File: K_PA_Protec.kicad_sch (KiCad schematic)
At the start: 89 parts, among them IC1 MCP23017_SO, J1 IDC 10 Straight, J10 MH2, J11 MH3, J12 MH4, J13 MH5, J14 MH6, J2 Molex KK 4, J3 IDC 10 Straight, J4 Molex KK 2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

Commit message: routing, first stage
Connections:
- net GND: now also SW1.2C, SW1.S1; no longer SW1.1C, SW1.S2
- net at J2.1 (Pin_1), R23.2: now also SW1.2A; no longer SW1.1A
- net at J2.2 (Pin_2), R5.2: now also SW1.2B; no longer SW1.1B
- net at J2.3 (Pin_3): now also SW1.S2; no longer SW1.S1
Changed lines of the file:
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@@
     (stroke (width 0) (type default) (color 0 0 0 0))
   )
-  (wire (pts (xy 55.245 186.69) (xy 56.515 186.69))
+  (wire (pts (xy 55.245 186.69) (xy 53.34 186.69))
     (stroke (width 0) (type default) (color 0 0 0 0))
   )
@@
     (stroke (width 0) (type default) (color 0 0 0 0))
   )
-  (wire (pts (xy 61.595 188.595) (xy 61.595 186.69))
-    (stroke (width 0) (type default) (color 0 0 0 0))
-  )
   (wire (pts (xy 131.445 17.78) (xy 132.715 17.78))
     (stroke (width 0) (type default) (color 0 0 0 0))
   )
+  (wire (pts (xy 41.91 188.595) (xy 60.325 188.595))
+    (stroke (width 0) (type default) (color 0 0 0 0))
+  )
   (wire (pts (xy 133.35 86.995) (xy 133.35 87.63))
     (stroke (width 0) (type default) (color 0 0 0 0))
@@
     (stroke (width 0) (type default) (color 0 0 0 0))
   )
+  (wire (pts (xy 60.325 186.69) (xy 60.325 188.595))
+    (stroke (width 0) (type default) (color 0 0 0 0))
+  )
   (wire (pts (xy 34.925 33.02) (xy 34.925 34.29))
     (stroke (width 0) (type default) (color 0 0 0 0))
@@
   )
   (wire (pts (xy 165.1 150.495) (xy 170.18 150.495))
-    (stroke (width 0) (type default) (color 0 0 0 0))
-  )
-  (wire (pts (xy 41.91 188.595) (xy 61.595 188.595))
     (stroke (width 0) (type default) (color 0 0 0 0))
   )
@@
     (pin "1")
   )
-  (symbol (lib_id "RotaryEncoder_Dual_Alps_EC11E-Switch_Vertical_H20mm:RotaryEncoder_Dual_Switch") (at 59.055 179.07 0) (unit 1)
-    (in_bom yes) (on_board yes) (fields_autoplaced)
-    (property "Reference" "SW1" (id 0) (at 59.055 170.0235 0))
-    (property "Value" "RotaryEncoder_Dual_Switch" (id 1) (at 59.055 172.7986 0))
-    (property "Footprint" "RotaryEncoder_Dual_Alps_EC11E-Switch_Vertical_H20mm:RotaryEncoder_Dual_Alps_EC11E-Switch_Vertical_H20mm" (id 2) (at 55.245 175.006 0)
-      (effects (font (size 1.27 1.27)) hide)
-    )
-    (property "Datasheet" "~" (id 3) (at 59.055 172.466 0)
+  (symbol (lib_id "RotaryEncoder_Dual_Alps_EC11E-Switch_Vertical_H20mm:RotaryEncoder_Dual_Switch") (at 57.785 179.07 0) (mirror y) (unit 1)
+    (in_bom yes) (on_board yes) (fields_autoplaced)
+    (property "Reference" "SW1" (id 0) (at 57.785 170.0235 0))
+    (property "Value" "RotaryEncoder_Dual_Switch" (id 1) (at 57.785 172.7986 0))
+    (property "Footprint" "RotaryEncoder_Dual_Alps_EC11E-Switch_Vertical_H20mm:RotaryEncoder_Dual_Alps_EC11E-Switch_Vertical_H20mm" (id 2) (at 61.595 175.006 0)
+      (effects (font (size 1.27 1.27)) hide)
+    )
+    (property "Datasheet" "~" (id 3) (at 57.785 172.466 0)
       (effects (font (size 1.27 1.27)) hide)
     )
@@
     (pin "9")
   )
-  (symbol (lib_id "power:GND") (at 55.245 186.69 270) (unit 1)
-    (in_bom yes) (on_board yes) (fields_autoplaced)
-    (property "Reference" "#PWR0173" (id 0) (at 48.895 186.69 0)
-      (effects (font (size 1.27 1.27)) hide)
-    )
-    (property "Value" "GND" (id 1) (at 55.88 187.169 90)
+  (symbol (lib_id "power:GND") (at 53.34 186.69 270) (mirror x) (unit 1)
+    (in_bom yes) (on_board yes) (fields_autoplaced)
+    (property "Reference" "#PWR0173" (id 0) (at 46.99 186.69 0)
+      (effects (font (size 1.27 1.27)) hide)
+    )
+    (property "Value" "GND" (id 1) (at 53.975 186.211 90)
       (effects (font (size 1.27 1.27)) (justify left))
     )
-    (property "Footprint" "" (id 2) (at 55.245 186.69 0)
-      (effects (font (size 1.27 1.27)) hide)
-    )
-    (property "Datasheet" "" (id 3) (at 55.245 186.69 0)
-      (effects (font (size 1.27 1.27)) hide)
-    )
+    (property "Footprint" "" (id 2) (at 53.34 186.69 0)
+      (effects (font (size 1.27 1.27)) hide)
+    )
+    (property "Datasheet" "" (id 3) (at 53.34 186.69 0)
+      (effects (font (size 1.27 1.27)) hide)
+    )

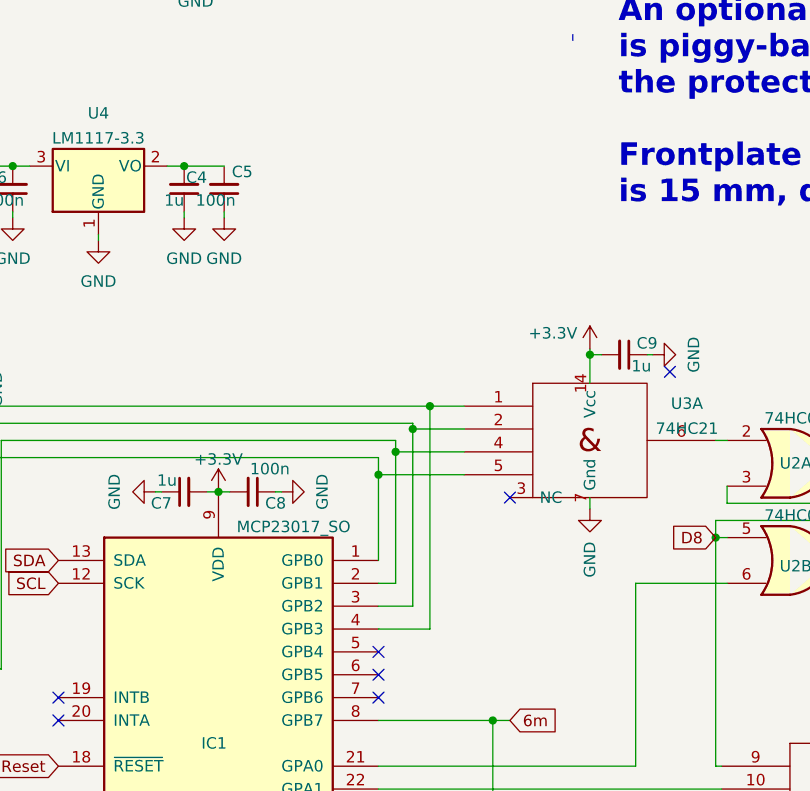
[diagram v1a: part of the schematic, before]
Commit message: routing completed, some minor changes expected
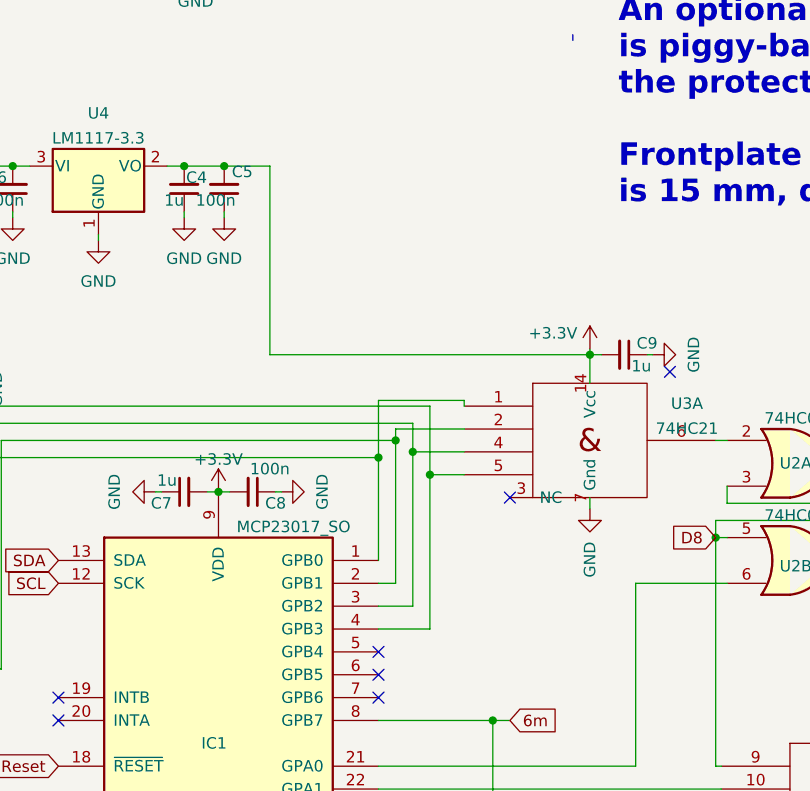
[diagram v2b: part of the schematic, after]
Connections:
- net +3V3: now also C4.2, C5.2, U4.2 (VO)
- net at IC1.3 (GPB2), R3.1, U1.13: now also U3.4; no longer U3.2
- net at IC1.2 (GPB1), R2.1, U1.1: now also U3.2; no longer U3.4
- net at IC1.1 (GPB0), R1.1, U1.2: now also U3.1; no longer U3.5
- net at IC1.4 (GPB3), R4.1, U1.14: now also U3.5; no longer U3.1
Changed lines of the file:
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@@
   (junction (at 41.91 133.985) (diameter 0) (color 0 0 0 0)
   )
-  (junction (at 135.255 85.09) (diameter 0) (color 0 0 0 0)
-  )
   (junction (at 45.72 141.605) (diameter 0) (color 0 0 0 0)
   )
@@
   (junction (at 234.95 27.305) (diameter 0) (color 0 0 0 0)
   )
-  (junction (at 129.54 92.71) (diameter 0) (color 0 0 0 0)
+  (junction (at 112.395 58.42) (diameter 0) (color 0 0 0 0)
+  )
+  (junction (at 133.35 90.17) (diameter 0) (color 0 0 0 0)
   )
   (junction (at 252.095 32.385) (diameter 0) (color 0 0 0 0)
@@
   (junction (at 46.355 119.38) (diameter 0) (color 0 0 0 0)
   )
+  (junction (at 129.54 90.805) (diameter 0) (color 0 0 0 0)
+  )
   (junction (at 142.24 120.015) (diameter 0) (color 0 0 0 0)
   )
@@
   (junction (at 84.455 58.42) (diameter 0) (color 0 0 0 0)
   )
+  (junction (at 135.255 92.71) (diameter 0) (color 0 0 0 0)
+  )
   (junction (at 243.205 32.385) (diameter 0) (color 0 0 0 0)
   )
@@
   (junction (at 49.53 103.505) (diameter 0) (color 0 0 0 0)
   )
-  (junction (at 133.35 87.63) (diameter 0) (color 0 0 0 0)
-  )
   (junction (at 107.95 58.42) (diameter 0) (color 0 0 0 0)
   )
-  (junction (at 131.445 90.17) (diameter 0) (color 0 0 0 0)
-  )
   (junction (at 134.62 149.225) (diameter 0) (color 0 0 0 0)
   )
@@
   )
   (junction (at 43.18 176.53) (diameter 0) (color 0 0 0 0)
+  )
+  (junction (at 131.445 88.9) (diameter 0) (color 0 0 0 0)
   )
   (junction (at 78.74 58.42) (diameter 0) (color 0 0 0 0)
@@
     (stroke (width 0) (type default) (color 0 0 0 0))
   )
-  (wire (pts (xy 133.35 87.63) (xy 139.065 87.63))
-    (stroke (width 0) (type default) (color 0 0 0 0))
-  )
   (wire (pts (xy 267.97 91.44) (xy 276.86 91.44))
     (stroke (width 0) (type default) (color 0 0 0 0))
@@
     (stroke (width 0) (type default) (color 0 0 0 0))
   )
+  (wire (pts (xy 133.35 90.17) (xy 139.065 90.17))
+    (stroke (width 0) (type default) (color 0 0 0 0))
+  )
   (wire (pts (xy 140.335 130.175) (xy 144.145 130.175))
     (stroke (width 0) (type default) (color 0 0 0 0))
@@
     (stroke (width 0) (type default) (color 0 0 0 0))
   )
-  (wire (pts (xy 131.445 90.17) (xy 139.065 90.17))
-    (stroke (width 0) (type default) (color 0 0 0 0))
-  )
   (wire (pts (xy 153.035 79.375) (xy 153.035 78.74))
     (stroke (width 0) (type default) (color 0 0 0 0))
@@
     (stroke (width 0) (type default) (color 0 0 0 0))
   )
-  (wire (pts (xy 135.255 85.09) (xy 139.065 85.09))
-    (stroke (width 0) (type default) (color 0 0 0 0))
-  )
   (wire (pts (xy 129.54 130.175) (xy 140.335 130.175))
     (stroke (width 0) (type default) (color 0 0 0 0))
@@
     (stroke (width 0) (type default) (color 0 0 0 0))
   )
+  (wire (pts (xy 117.475 58.42) (xy 117.475 79.375))
+    (stroke (width 0) (type default) (color 0 0 0 0))
+  )
   (wire (pts (xy 87.63 88.9) (xy 131.445 88.9))
     (stroke (width 0) (type default) (color 0 0 0 0))
   )
+  (wire (pts (xy 129.54 84.455) (xy 129.54 90.805))
+    (stroke (width 0) (type default) (color 0 0 0 0))
+  )
   (wire (pts (xy 130.81 142.875) (xy 144.145 142.875))
     (stroke (width 0) (type default) (color 0 0 0 0))
@@
     (stroke (width 0) (type default) (color 0 0 0 0))
   )
+  (wire (pts (xy 139.065 85.09) (xy 139.065 84.455))
+    (stroke (width 0) (type default) (color 0 0 0 0))
+  )
   (wire (pts (xy 231.775 24.765) (xy 236.855 24.765))
     (stroke (width 0) (type default) (color 0 0 0 0))
@@
     (stroke (width 0) (type default) (color 0 0 0 0))
   )
+  (wire (pts (xy 133.35 90.17) (xy 133.35 107.315))
+    (stroke (width 0) (type default) (color 0 0 0 0))
+  )
   (wire (pts (xy 195.58 120.65) (xy 195.58 128.905))
     (stroke (width 0) (type default) (color 0 0 0 0))
@@
     (stroke (width 0) (type default) (color 0 0 0 0))
   )
-  (wire (pts (xy 133.35 87.63) (xy 133.35 107.315))
+  (wire (pts (xy 133.35 86.995) (xy 133.35 90.17))
     (stroke (width 0) (type default) (color 0 0 0 0))
   )
@@
     (stroke (width 0) (type default) (color 0 0 0 0))
   )
-  (wire (pts (xy 135.255 85.09) (xy 135.255 109.855))
+  (wire (pts (xy 135.255 85.09) (xy 135.255 92.71))
     (stroke (width 0) (type default) (color 0 0 0 0))
   )
@@
     (stroke (width 0) (type default) (color 0 0 0 0))
   )
+  (wire (pts (xy 139.065 87.63) (xy 131.445 87.63))
+    (stroke (width 0) (type default) (color 0 0 0 0))
+  )
   (wire (pts (xy 131.445 36.83) (xy 132.715 36.83))
     (stroke (width 0) (type default) (color 0 0 0 0))
@@
     (stroke (width 0) (type default) (color 0 0 0 0))
   )
-  (wire (pts (xy 129.54 92.71) (xy 139.065 92.71))
-    (stroke (width 0) (type default) (color 0 0 0 0))
-  )
   (wire (pts (xy 83.82 156.845) (xy 83.82 85.09))
     (stroke (width 0) (type default) (color 0 0 0 0))
@@
     (stroke (width 0) (type default) (color 0 0 0 0))
   )
+  (wire (pts (xy 131.445 87.63) (xy 131.445 88.9))
+    (stroke (width 0) (type default) (color 0 0 0 0))
+  )
   (wire (pts (xy 41.91 188.595) (xy 60.325 188.595))
     (stroke (width 0) (type default) (color 0 0 0 0))
   )
-  (wire (pts (xy 133.35 86.995) (xy 133.35 87.63))
-    (stroke (width 0) (type default) (color 0 0 0 0))
-  )
   (wire (pts (xy 93.98 142.875) (xy 93.98 143.51))
     (stroke (width 0) (type default) (color 0 0 0 0))
@@
     (stroke (width 0) (type default) (color 0 0 0 0))
   )
-  (wire (pts (xy 129.54 90.805) (xy 129.54 92.71))
-    (stroke (width 0) (type default) (color 0 0 0 0))
-  )
-  (wire (pts (xy 129.54 92.71) (xy 129.54 102.235))
+  (wire (pts (xy 129.54 90.805) (xy 129.54 102.235))
     (stroke (width 0) (type default) (color 0 0 0 0))
   )
@@
     (stroke (width 0) (type default) (color 0 0 0 0))
   )
+  (wire (pts (xy 135.255 92.71) (xy 139.065 92.71))
+    (stroke (width 0) (type default) (color 0 0 0 0))
+  )
   (wire (pts (xy 37.465 93.345) (xy 37.465 90.805))
     (stroke (width 0) (type default) (color 0 0 0 0))
@@
     (stroke (width 0) (type default) (color 0 0 0 0))
   )
+  (wire (pts (xy 135.255 92.71) (xy 135.255 109.855))
+    (stroke (width 0) (type default) (color 0 0 0 0))
+  )
   (wire (pts (xy 88.9 58.42) (xy 90.805 58.42))
     (stroke (width 0) (type default) (color 0 0 0 0))
@@
     (stroke (width 0) (type default) (color 0 0 0 0))
   )
+  (wire (pts (xy 112.395 58.42) (xy 117.475 58.42))
+    (stroke (width 0) (type default) (color 0 0 0 0))
+  )
   (wire (pts (xy 76.835 106.68) (xy 76.835 128.905))
     (stroke (width 0) (type default) (color 0 0 0 0))
   )
+  (wire (pts (xy 117.475 79.375) (xy 153.035 79.375))
+    (stroke (width 0) (type default) (color 0 0 0 0))
+  )
   (wire (pts (xy 107.95 63.5) (xy 107.95 64.135))
     (stroke (width 0) (type default) (color 0 0 0 0))
@@
     (stroke (width 0) (type default) (color 0 0 0 0))
   )
+  (wire (pts (xy 139.065 84.455) (xy 129.54 84.455))
+    (stroke (width 0) (type default) (color 0 0 0 0))
+  )
   (wire (pts (xy 241.935 40.005) (xy 242.57 40.005))
     (stroke (width 0) (type default) (color 0 0 0 0))
@@
     (stroke (width 0) (type default) (color 0 0 0 0))
   )
-  (wire (pts (xy 131.445 90.17) (xy 131.445 104.775))
+  (wire (pts (xy 131.445 88.9) (xy 131.445 104.775))
     (stroke (width 0) (type default) (color 0 0 0 0))
   )
@@
     (stroke (width 0) (type default) (color 0 0 0 0))
   )
-  (wire (pts (xy 131.445 88.9) (xy 131.445 90.17))
-    (stroke (width 0) (type default) (color 0 0 0 0))
-  )

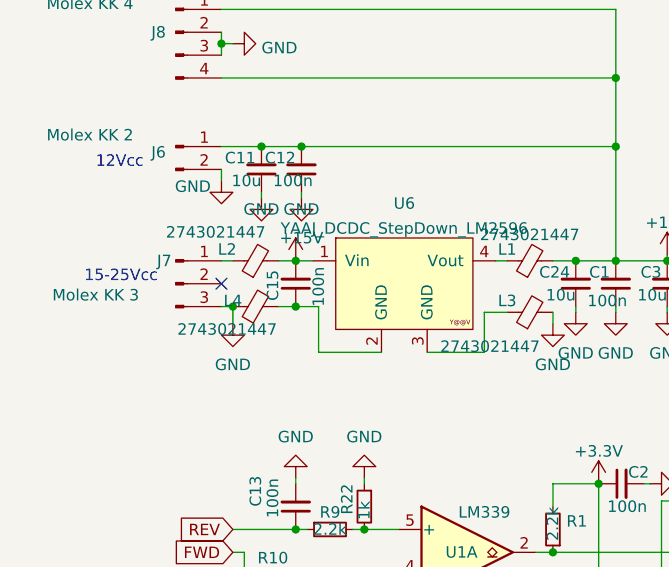
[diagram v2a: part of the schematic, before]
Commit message: small layout mods
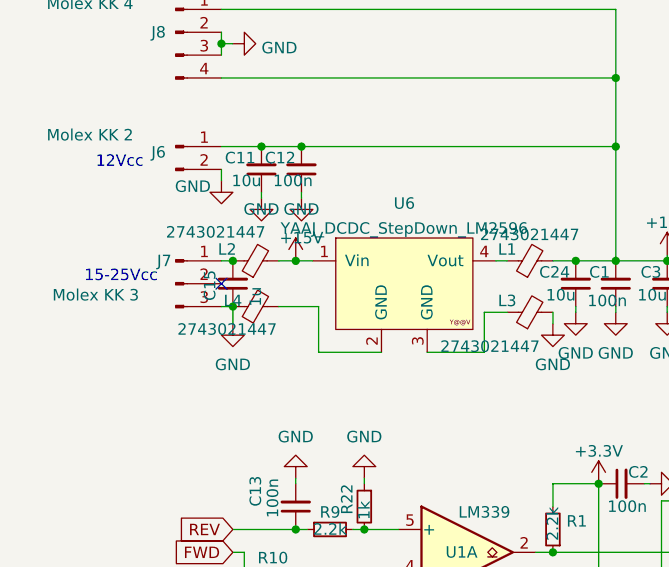
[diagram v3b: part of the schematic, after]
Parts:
- C15: value 100n -> 1u
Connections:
- net +15V: no longer C15.2
- net GND: now also C15.1
- net at J7.1 (Pin_1), L2.1: now also C15.2
- net at L4.2, U6.2 (GND): no longer C15.1
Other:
- moved on the sheet: C15
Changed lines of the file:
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@@
   (junction (at 252.095 32.385) (diameter 0) (color 0 0 0 0)
   )
-  (junction (at 43.18 63.5) (diameter 0) (color 0 0 0 0)
-  )
   (junction (at 46.355 119.38) (diameter 0) (color 0 0 0 0)
   )
@@
   (junction (at 46.99 161.925) (diameter 0) (color 0 0 0 0)
   )
+  (junction (at 36.195 58.42) (diameter 0) (color 0 0 0 0)
+  )
   (junction (at 234.95 29.845) (diameter 0) (color 0 0 0 0)
   )
@@
     (stroke (width 0) (type default) (color 0 0 0 0))
   )
-  (wire (pts (xy 45.72 63.5) (xy 43.18 63.5))
+  (wire (pts (xy 41.275 63.5) (xy 45.72 63.5))
     (stroke (width 0) (type default) (color 0 0 0 0))
   )
@@
     (stroke (width 0) (type default) (color 0 0 0 0))
   )
-  (wire (pts (xy 64.135 64.135) (xy 66.675 64.135))
-    (stroke (width 0) (type default) (color 0 0 0 0))
-  )
   (wire (pts (xy 243.205 32.385) (xy 252.095 32.385))
     (stroke (width 0) (type default) (color 0 0 0 0))
@@
     (stroke (width 0) (type default) (color 0 0 0 0))
   )
-  (polyline (pts (xy 151.13 43.815) (xy 151.13 44.45))
+  (wire (pts (xy 64.135 64.135) (xy 66.675 64.135))
     (stroke (width 0) (type default) (color 0 0 0 0))
   )
-  (wire (pts (xy 183.515 95.885) (xy 183.515 102.235))
+  (polyline (pts (xy 151.13 43.815) (xy 151.13 44.45))
     (stroke (width 0) (type default) (color 0 0 0 0))
   )
-  (wire (pts (xy 41.275 63.5) (xy 43.18 63.5))
+  (wire (pts (xy 183.515 95.885) (xy 183.515 102.235))
     (stroke (width 0) (type default) (color 0 0 0 0))
   )
@@
     (pin "9")
   )
-  (symbol (lib_id "Device:C_Small") (at 43.18 60.96 0) (mirror x) (unit 1)
+  (symbol (lib_id "Device:C_Small") (at 36.195 60.96 0) (mirror x) (unit 1)
     (in_bom yes) (on_board yes)
-    (property "Reference" "C15" (id 0) (at 40.64 62.865 90)
+    (property "Reference" "C15" (id 0) (at 33.655 62.865 90)
       (effects (font (size 1.27 1.27)) (justify right))
     )
-    (property "Value" "100n" (id 1) (at 45.72 63.5 90)
+    (property "Value" "1u" (id 1) (at 38.735 63.5 90)
       (effects (font (size 1.27 1.27)) (justify right))
     )
-    (property "Footprint" "Capacitor_SMD:C_0805_2012Metric_Pad1.18x1.45mm_HandSolder" (id 2) (at 43.18 60.96 0)
+    (property "Footprint" "Capacitor_SMD:C_0805_2012Metric_Pad1.18x1.45mm_HandSolder" (id 2) (at 36.195 60.96 0)
       (effects (font (size 1.27 1.27)) hide)
     )
-    (property "Datasheet" "~" (id 3) (at 43.18 60.96 0)
+    (property "Datasheet" "~" (id 3) (at 36.195 60.96 0)
       (effects (font (size 1.27 1.27)) hide)
     )
@@
     )
     (path "/b446581f-a7d8-4173-894c-9d5efb00b443"
-      (reference "C15") (unit 1) (value "100n") (footprint "Capacitor_SMD:C_0805_2012Metric_Pad1.18x1.45mm_HandSolder")
+      (reference "C15") (unit 1) (value "1u") (footprint "Capacitor_SMD:C_0805_2012Metric_Pad1.18x1.45mm_HandSolder")
     )
     (path "/21f0d037-e01b-4c76-81cd-bae41e57f30b"

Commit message: silkscreen cleanup, small routing mods
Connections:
- net +12V_A is gone; now on net +12V: J3.4 (Pin_4)
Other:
- note added: "To Antenna board"
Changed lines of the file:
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@@
   (junction (at 133.35 90.17) (diameter 0) (color 0 0 0 0)
   )
+  (junction (at 269.24 91.44) (diameter 0) (color 0 0 0 0)
+  )
   (junction (at 252.095 32.385) (diameter 0) (color 0 0 0 0)
   )
@@
     (stroke (width 0) (type default) (color 0 0 0 0))
   )
-  (wire (pts (xy 267.97 91.44) (xy 276.86 91.44))
+  (wire (pts (xy 267.97 91.44) (xy 269.24 91.44))
     (stroke (width 0) (type default) (color 0 0 0 0))
   )
@@
     (stroke (width 0) (type default) (color 0 0 0 0))
   )
+  (wire (pts (xy 269.24 91.44) (xy 276.86 91.44))
+    (stroke (width 0) (type default) (color 0 0 0 0))
+  )
   (wire (pts (xy 129.54 135.255) (xy 136.525 135.255))
     (stroke (width 0) (type default) (color 0 0 0 0))
@@
     (effects (font (size 1.27 1.27) bold) (justify left bottom))
   )
+  (text "To Antenna board\n" (at 284.48 113.665 90)
+    (effects (font (size 1.27 1.27)) (justify left bottom))
+  )
   (text "vérifier empreinte inductance choke\n\nvérifier empreinte trimmers 1k\n\nvérifier C3 C11 C24"
     (at 213.995 81.915 0)
@@
     (pin "2")
   )
+  (symbol (lib_id "power:+12V") (at 269.24 91.44 0) (unit 1)
+    (in_bom yes) (on_board yes) (fields_autoplaced)
+    (property "Reference" "#PWR0134" (id 0) (at 269.24 95.25 0)
+      (effects (font (size 1.27 1.27)) hide)
+    )
+    (property "Value" "+12V" (id 1) (at 269.24 87.8355 0))
+    (property "Footprint" "" (id 2) (at 269.24 91.44 0)
+      (effects (font (size 1.27 1.27)) hide)
+    )
+    (property "Datasheet" "" (id 3) (at 269.24 91.44 0)
+      (effects (font (size 1.27 1.27)) hide)
+    )
+    (pin "1")
+  )
   (symbol (lib_id "power:GND") (at 36.83 184.15 90) (unit 1)
     (in_bom yes) (on_board yes) (fields_autoplaced)
@@
       (reference "#PWR0133") (unit 1) (value "GND") (footprint "")
     )
+    (path "/9887f452-3a43-4590-8499-a866d3c2a535"
+      (reference "#PWR0134") (unit 1) (value "+12V") (footprint "")
+    )
     (path "/2842afa2-e900-40a7-89c1-88bde4b18cff"
